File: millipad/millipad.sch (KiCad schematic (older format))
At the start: 47 parts, among them SW1 SW_Push, SW2 Rotary_Encoder_Switch, U1 ATmega32U4-AU, U2 PRTR5V0U2X, Y1 16MHz

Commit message: PCB Layout
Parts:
- added H1, H2, H3, H4: MountingHole, MountingHole:MountingHole_2.7mm_M2.5, symbol Mechanical:MountingHole
- C1, C2, C3, C4, C5, C6, C7, C8, C9: footprint (none) -> Capacitor_SMD:C_0805_2012Metric
- D1, D10, D11, D12, D13, D2, D3, D4, D5, D6, D7, D8, D9: footprint (none) -> Diode_SMD:D_SOD-123
- F1: footprint (none) -> Fuse:Fuse_1206_3216Metric
- MX1, MX10, MX11, MX12, MX2, MX3, MX4, MX5, MX6, MX7, MX8, MX9: footprint (none) -> MX_Only:MXOnly-1U-Hotswap
- R1, R2, R3, R4, R5, R6: footprint (none) -> Resistor_SMD:R_0805_2012Metric
- SW1: footprint (none) -> random-keyboard-parts:SKQG-1155865
- SW2: footprint (none) -> Keebio-Parts:RotaryEncoder_Alps_EC11E-Switch_Vertical_H20mm
- U2: footprint (none) -> prtr5v:PRTR5V0U2X
- USB1: footprint (none) -> Type-C:HRO-TYPE-C-31-M-12-HandSoldering
- Y1: footprint (none) -> Crystal:Crystal_SMD_3225-4Pin_3.2x2.5mm
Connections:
- net COL0: now also U1.41 (PF0); no longer U1.20 (PD2)
- net COL1: now also U1.40 (PF1); no longer U1.21 (PD3)
- net COL2: now also U1.39 (PF4); no longer U1.25 (PD4)
- net COL3: now also U1.27 (PD7); no longer U1.22 (PD5)
- net COL5: now also U1.25 (PD4); no longer U1.27 (PD7)
- net COL6: now also U1.22 (PD5); no longer U1.32 (PC7)
- net ENC_A: now also U1.20 (PD2)
- net ENC_B: now also U1.21 (PD3)
- net ROW0: now also U1.31 (PC6); no longer U1.18 (PD0)
- net ROW1: now also U1.32 (PC7); no longer U1.19 (PD1)

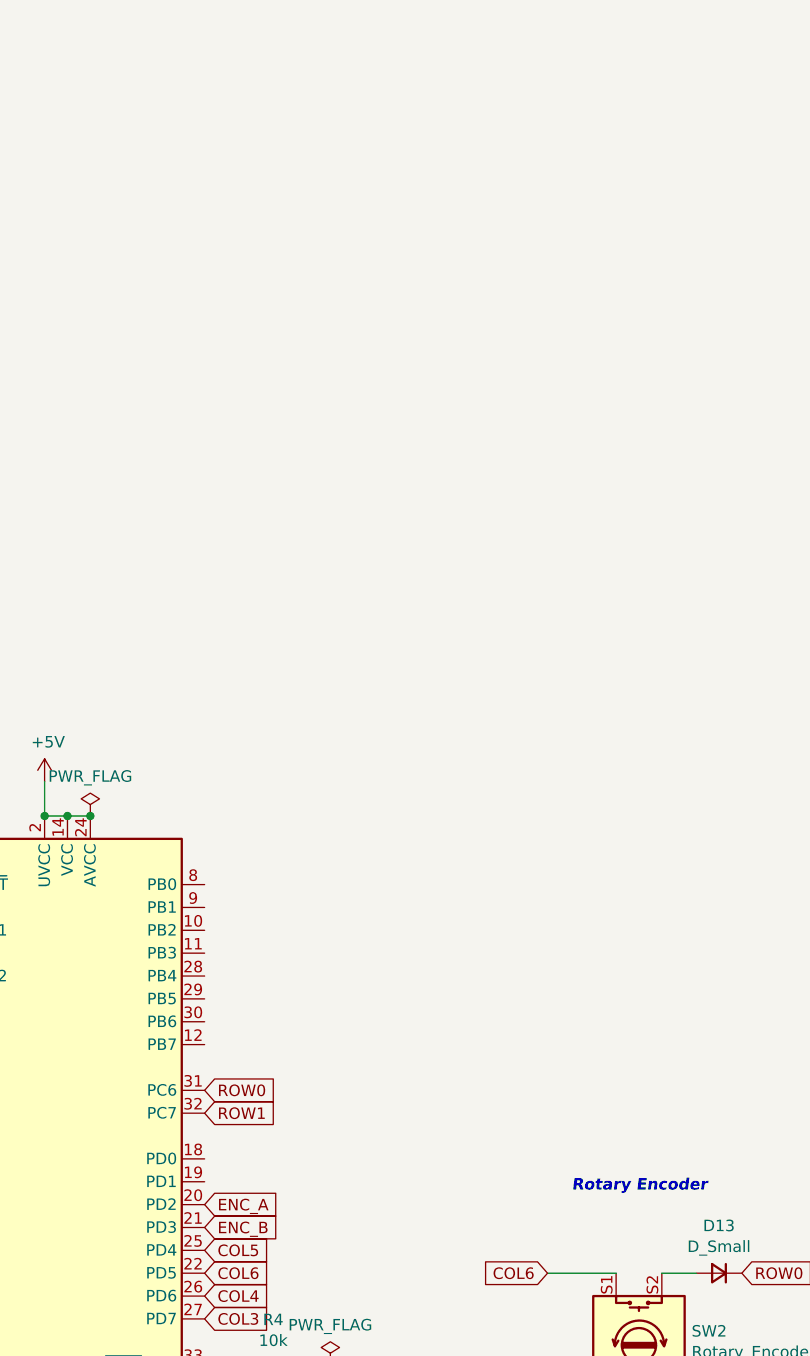
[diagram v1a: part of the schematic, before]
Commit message: Added SSD1306 128x64 OLED Breakout Board
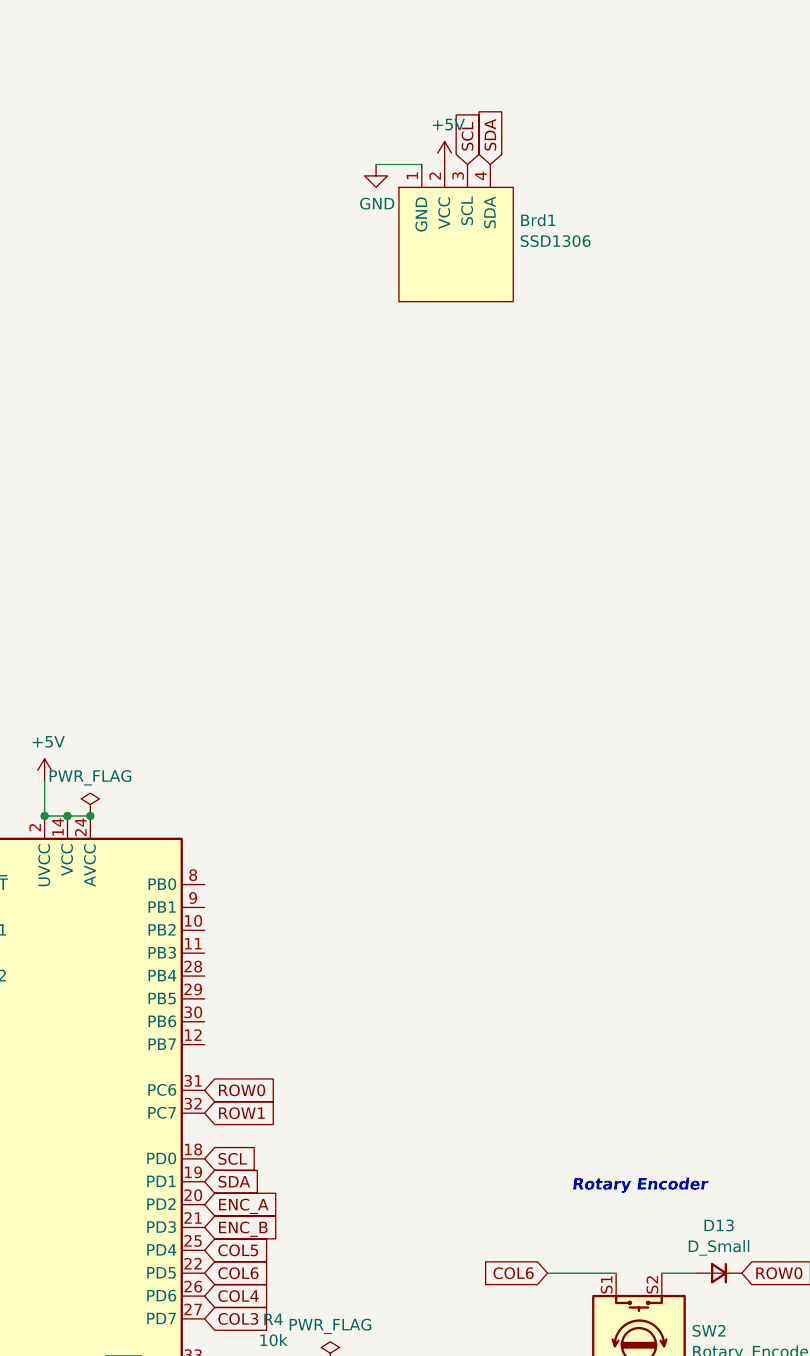
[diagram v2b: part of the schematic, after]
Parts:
- added Brd1: SSD1306, SSD1306:128x64OLED, symbol SSD1306-128x64_OLED:SSD1306
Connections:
- net +5V: now also Brd1.2 (VCC)
- net GND: now also Brd1.1 (GND)
- net SCL: now reaches U1.18 (PD0)
- net SCL: now also Brd1.3 (SCL)
- net SDA: now reaches U1.19 (PD1)
- net SDA: now also Brd1.4 (SDA)
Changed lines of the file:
@@
+	1    0    0    -1
+$EndComp
+$Comp
+L SSD1306-128x64_OLED:SSD1306 Brd1
+U 1 1 6066316E
+P 4600 1500
+F 0 "Brd1" H 4878 1604 50  0000 L CNN
+F 1 "SSD1306" H 4878 1513 50  0000 L CNN
+F 2 "SSD1306:128x64OLED" H 4600 1750 50  0001 C CNN
+F 3 "" H 4600 1750 50  0001 C CNN
+	1    4600 1500
+	1    0    0    -1
+$EndComp
+Text GLabel 3500 5500 2    50   Input ~ 0
+SCL
+Text GLabel 3500 5600 2    50   Input ~ 0
+SDA
+Text GLabel 4650 1150 1    50   Input ~ 0
+SCL
+Text GLabel 4750 1150 1    50   Input ~ 0
+SDA
+$Comp
+L power:GND #PWR0102
+U 1 1 60675E47
+P 4250 1150
+F 0 "#PWR0102" H 4250 900 50  0001 C CNN
+F 1 "GND" H 4255 977 50  0000 C CNN
+F 2 "" H 4250 1150 50  0001 C CNN
+F 3 "" H 4250 1150 50  0001 C CNN
+	1    4250 1150
+	1    0    0    -1
+$EndComp
+Wire Wire Line
+	4250 1150 4450 1150
+$Comp
+L power:+5V #PWR?
+U 1 1 606B5B8A
+P 4550 1150
+F 0 "#PWR?" H 4550 1000 50  0001 C CNN
+F 1 "+5V" H 4565 1323 50  0000 C CNN
+F 2 "" H 4550 1150 50  0001 C CNN
+F 3 "" H 4550 1150 50  0001 C CNN
+	1    4550 1150
 	1    0    0    -1
 $EndComp

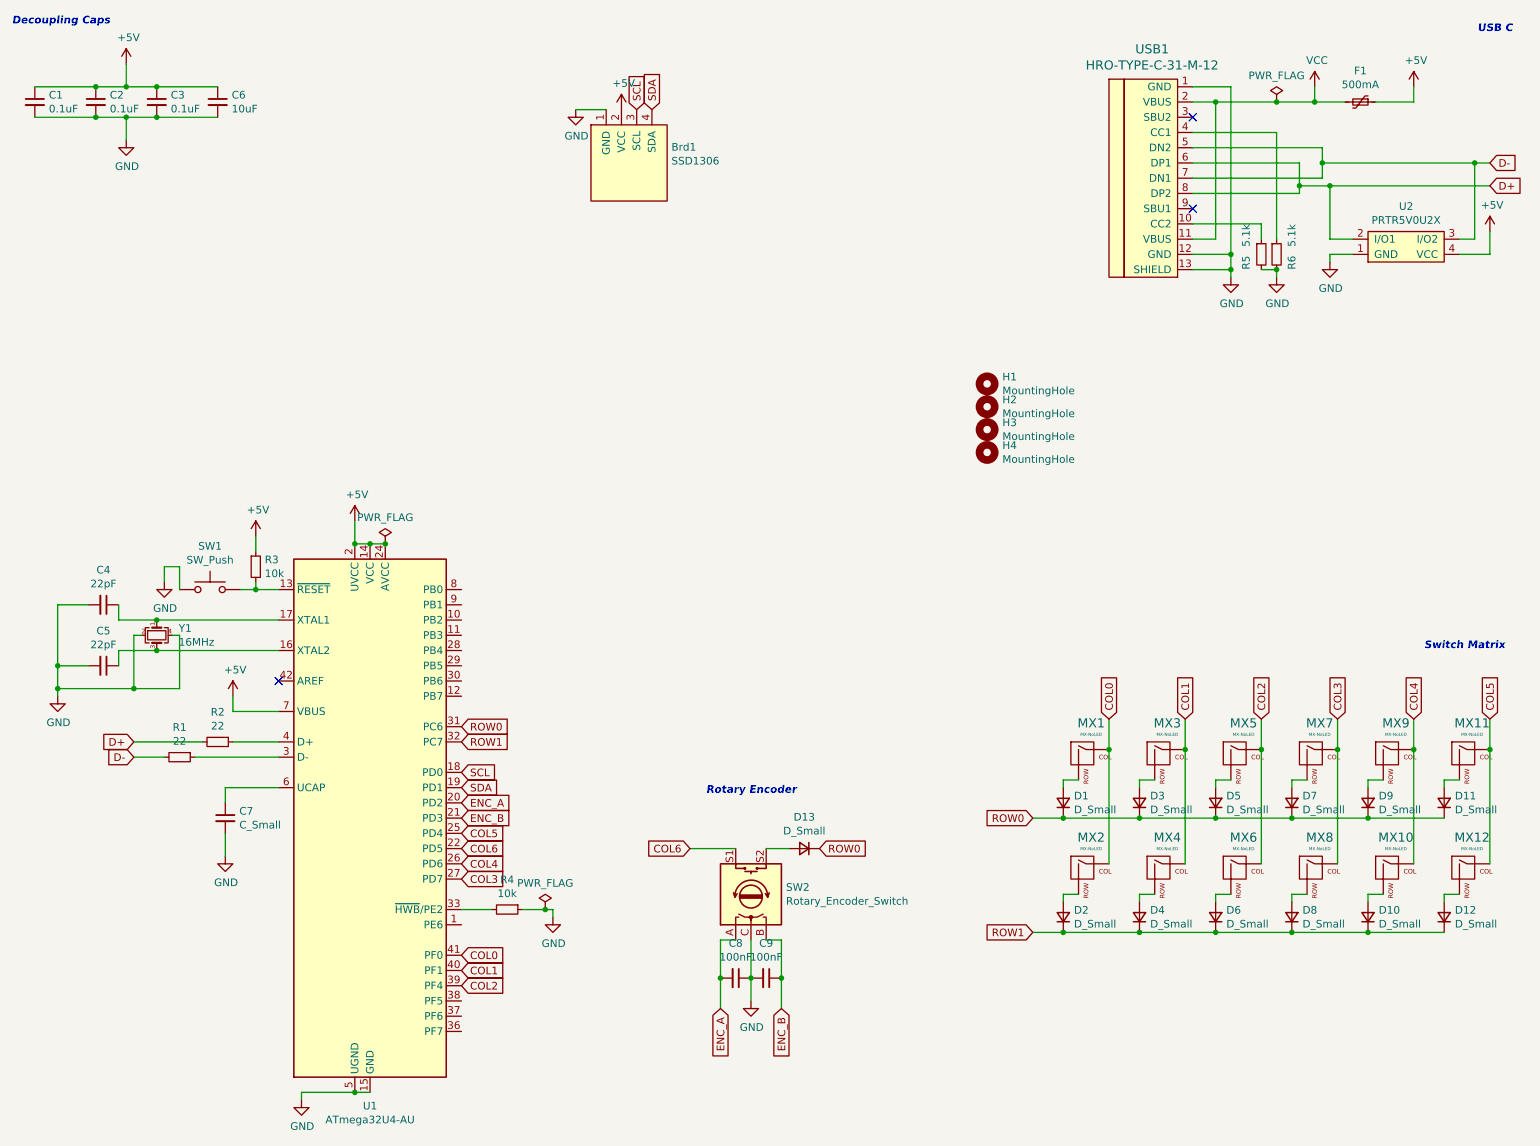
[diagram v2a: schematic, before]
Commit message: Added pushbutton and isp flash headers
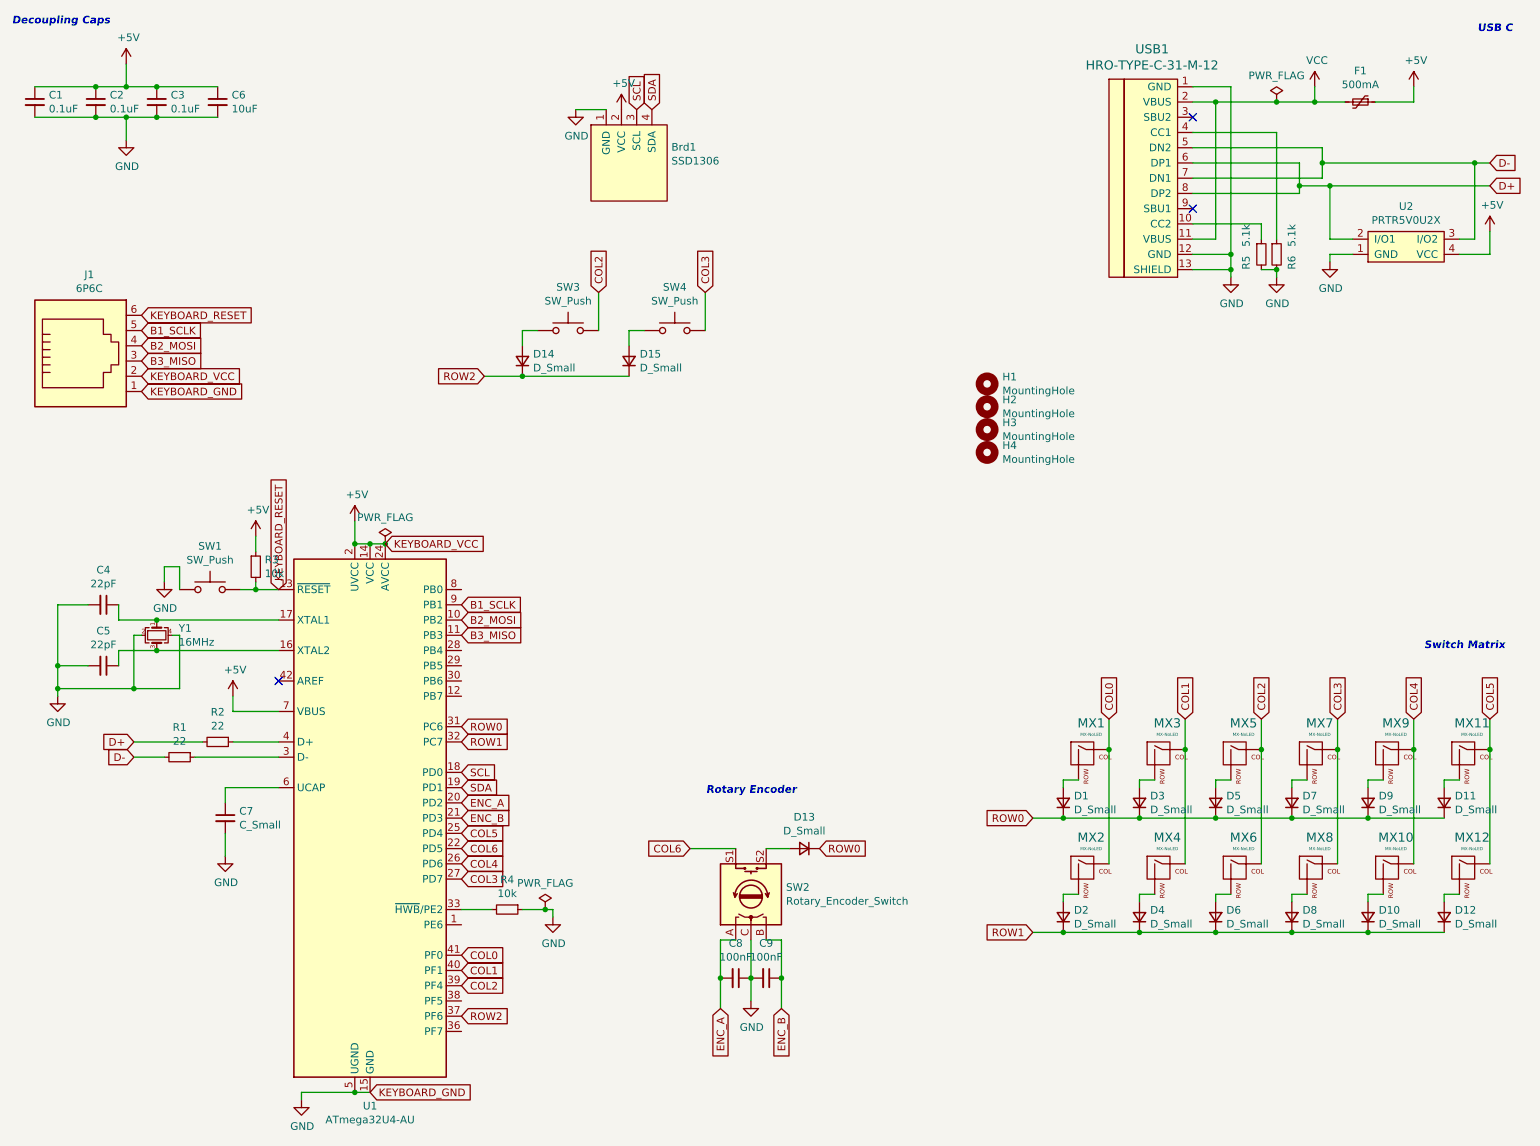
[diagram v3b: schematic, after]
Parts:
- added D14, D15: D_Small, Diode_SMD:D_SOD-123, symbol Device:D_Small
- added J1: 6P6C, Connector_PinSocket_1.00mm:PinSocket_2x03_P1.00mm_Vertical_SMD, symbol Connector:6P6C
- added SW3, SW4: SW_Push, random-keyboard-parts:SKQG-1155865, symbol Switch:SW_Push
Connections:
- net +5V: now also J1.2
- net COL2: now also SW3.2
- net COL3: now also SW4.2
- net GND: now also J1.1
- net B2_MOSI: now reaches U1.10 (PB2)
- net B2_MOSI: now also J1.4
- net B3_MISO: now reaches U1.11 (PB3)
- net B3_MISO: now also J1.3
- net KEYBOARD_RESET: now reaches R3.2, SW1.2, U1.13 (~RESET)
- net KEYBOARD_RESET: now also J1.6
- net ROW2: now reaches U1.37 (PF6)
- net ROW2: now also D14.1 (K), D15.1 (K)
- net B1_SCLK: now reaches U1.9 (PB1)
- net B1_SCLK: now also J1.5
- new net: D14.2 (A), SW3.1
- new net: D15.2 (A), SW4.1
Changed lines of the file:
@@
 	4250 1150 4450 1150
 $Comp
-L power:+5V #PWR?
+L power:+5V #PWR0101
 U 1 1 606B5B8A
 P 4550 1150
-F 0 "#PWR?" H 4550 1000 50  0001 C CNN
+F 0 "#PWR0101" H 4550 1000 50  0001 C CNN
 F 1 "+5V" H 4565 1323 50  0000 C CNN
 F 2 "" H 4550 1150 50  0001 C CNN
@@
 	1    0    0    -1
 $EndComp
+$Comp
+L Connector:6P6C J1
+U 1 1 606D5F68
+P 1000 2800
+F 0 "J1" H 1057 3367 50  0000 C CNN
+F 1 "6P6C" H 1057 3276 50  0000 C CNN
+F 2 "Connector_PinSocket_1.00mm:PinSocket_2x03_P1.00mm_Vertical_SMD" V 1000 2825 50  0001 C CNN
+F 3 "~" V 1000 2825 50  0001 C CNN
+	1    1000 2800
+	1    0    0    -1
+$EndComp
+Text GLabel 1400 3000 2    50   Input ~ 0
+KEYBOARD_GND
+Text GLabel 1400 2900 2    50   Input ~ 0
+KEYBOARD_VCC
+Text GLabel 1400 2800 2    50   Input ~ 0
+B3_MISO
+Text GLabel 1400 2700 2    50   Input ~ 0
+B2_MOSI
+Text GLabel 1400 2600 2    50   Input ~ 0
+B1_SCLK
+Text GLabel 1400 2500 2    50   Input ~ 0
+KEYBOARD_RESET
+Text GLabel 2300 4300 1    50   Input ~ 0
+KEYBOARD_RESET
+Text GLabel 3000 4000 2    50   Input ~ 0
+KEYBOARD_VCC
+Text GLabel 2900 7600 2    50   Input ~ 0
+KEYBOARD_GND
+Text GLabel 3500 4400 2    50   Input ~ 0
+B1_SCLK
+Text GLabel 3500 4500 2    50   Input ~ 0
+B2_MOSI
+Text GLabel 3500 4600 2    50   Input ~ 0
+B3_MISO
+$Comp
+L Switch:SW_Push SW3
+U 1 1 60701A5F
+P 4200 2600
+F 0 "SW3" H 4200 2885 50  0000 C CNN
+F 1 "SW_Push" H 4200 2794 50  0000 C CNN
+F 2 "random-keyboard-parts:SKQG-1155865" H 4200 2800 50  0001 C CNN
+F 3 "~" H 4200 2800 50  0001 C CNN
+	1    4200 2600
+	1    0    0    -1
+$EndComp
+$Comp
+L Switch:SW_Push SW4
+U 1 1 60703032
+P 4900 2600
+F 0 "SW4" H 4900 2885 50  0000 C CNN
+F 1 "SW_Push" H 4900 2794 50  0000 C CNN
+F 2 "random-keyboard-parts:SKQG-1155865" H 4900 2800 50  0001 C CNN
+F 3 "~" H 4900 2800 50  0001 C CNN
+	1    4900 2600
+	1    0    0    -1
+$EndComp
+$Comp
+L Device:D_Small D14
+U 1 1 60704EFB
+P 3900 2800
+F 0 "D14" V 3946 2730 50  0000 R CNN
+F 1 "D_Small" V 3855 2730 50  0000 R CNN
+F 2 "Diode_SMD:D_SOD-123" V 3900 2800 50  0001 C CNN
+F 3 "~" V 3900 2800 50  0001 C CNN
+	1    3900 2800
+	0    -1   -1   0
+$EndComp
+$Comp
+L Device:D_Small D15
+U 1 1 60705388
+P 4600 2800
+F 0 "D15" V 4646 2730 50  0000 R CNN
+F 1 "D_Small" V 4555 2730 50  0000 R CNN
+F 2 "Diode_SMD:D_SOD-123" V 4600 2800 50  0001 C CNN
+F 3 "~" V 4600 2800 50  0001 C CNN
+	1    4600 2800
+	0    -1   -1   0
+$EndComp
+Wire Wire Line
+	4700 2600 4600 2600
+Wire Wire Line
+	4600 2600 4600 2700
+Wire Wire Line
+	4000 2600 3900 2600
+Wire Wire Line
+	3900 2600 3900 2700
+Wire Wire Line
+	4600 2900 3900 2900
+Connection ~ 3900 2900
+Wire Wire Line
+	3900 2900 3650 2900
+Wire Wire Line
+	4400 2350 4400 2600
+Wire Wire Line
+	5100 2350 5100 2600
+Text GLabel 3650 2900 0    50   Input ~ 0
+ROW2
+Text GLabel 4400 2350 1    50   Input ~ 0
+COL2
+Text GLabel 5100 2350 1    50   Input ~ 0
+COL3
+Text GLabel 3500 7100 2    50   Input ~ 0
+ROW2
 $EndSCHEMATC

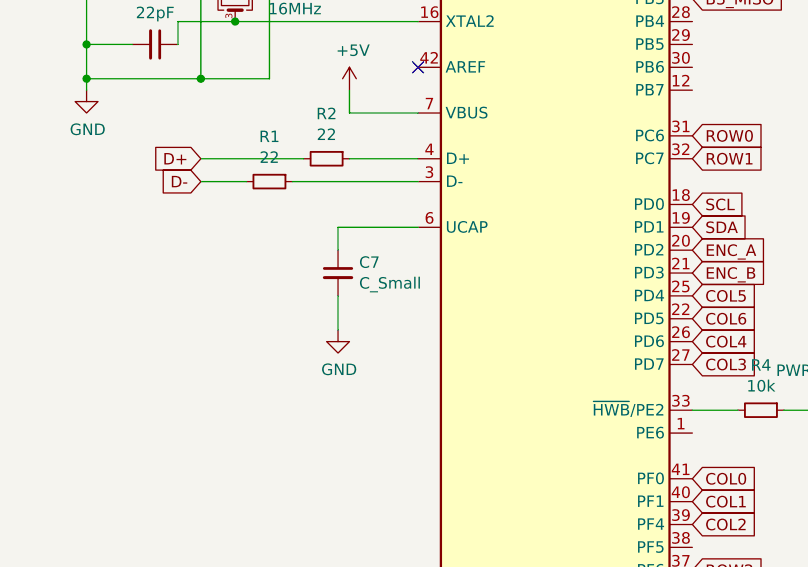
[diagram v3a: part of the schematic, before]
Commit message: Generated BOM, POS, STEP for Plate Assembly
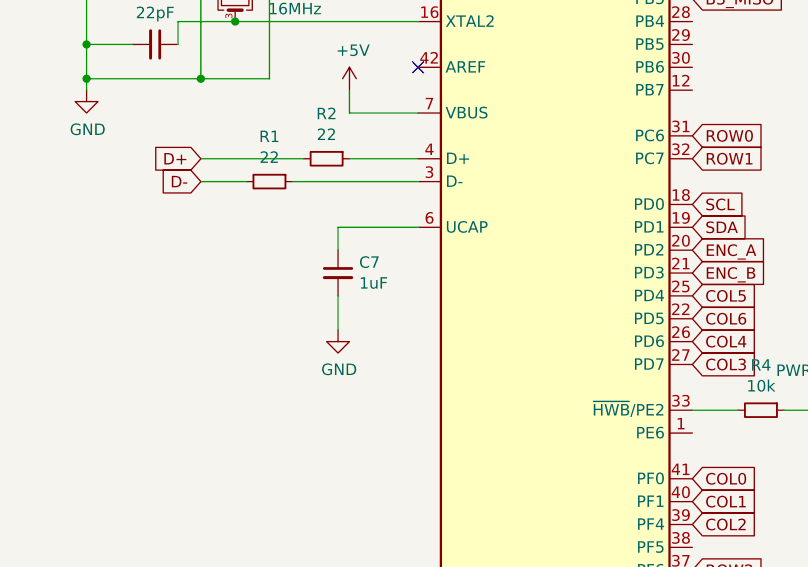
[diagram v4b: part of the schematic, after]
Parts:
- C7: value C_Small -> 1uF
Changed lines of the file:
@@
 P 1950 5800
 F 0 "C7" H 2042 5846 50  0000 L CNN
-F 1 "C_Small" H 2042 5755 50  0000 L CNN
+F 1 "1uF" H 2042 5755 50  0000 L CNN
 F 2 "Capacitor_SMD:C_0805_2012Metric" H 1950 5800 50  0001 C CNN
 F 3 "~" H 1950 5800 50  0001 C CNN
